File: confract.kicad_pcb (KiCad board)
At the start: 2 copper layers, 44 parts, among them J1 Conn_01x05, J10 GS2, J11 Conn_01x04, J12 GS2, J13 GS2, J14 GS2, J15 GS2, J16 Conn_01x02, J2 GS3, J3 Conn_01x05, J4 GS3, J5 Audio-Jack-4, J6 GS2, J7 GS2, J8 GS2, J9 GS3, Q1 Q_NMOS_GSD, SW1 SW_Push, SW10 SW_Push, SW11 SW_Push, SW12 SW_Push, SW13 SW_Push, SW14 SW_Push, SW15 SW_Push, SW16 SW_Push, SW17 SW_Push, SW2 SW_Push, SW3 SW_Push, SW4 SW_Push, SW5 SW_Push, SW6 SW_Push, SW7 SW_Push, SW8 SW_Push, SW9 SW_Push, U1 MCP23017_QFN

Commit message: load pcb-outline
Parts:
- moved J14 201.3 mm to (339.5, 76.8)
- moved J8 200.9 mm to (340.1, 87.0)
- moved J13 200.9 mm to (339.5, 80.2)
- moved J10 200.6 mm to (339.5, 83.6)
- moved J2 200.6 mm to (340.0, 91.1)
- moved C1 200.4 mm to (338.0, 71.8)
- moved U1 191.9 mm to (331.3, 92.4)
- moved SW2 190.5 mm to (328.7, 76.6)
- moved J6 188.5 mm to (328.1, 99.5)
- moved J1 181.2 mm to (320.6, 90.4)
- moved J4 177.7 mm to (316.8, 113.0)
- moved R6 177.6 mm to (317.1, 107.3)
- moved SW4 173.9 mm to (311.9, 76.6)
- moved Q1 172.0 mm to (309.7, 125.5)
- moved J5 170.6 mm to (310.2, 97.1)
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
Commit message: place components
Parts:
- J12, J13, J14, J15, J16: moved to B.Cu
- moved SW2 248.8 mm to (79.9, 70.0)
- moved SW4 234.1 mm to (80.0, 108.0)
- moved SW3 218.0 mm to (79.9, 89.0)
- moved J2 206.7 mm to (133.3, 93.3)
- moved C1 205.3 mm to (134.5, 98.5)
- moved U1 203.9 mm to (127.5, 98.5), turned to 135 degrees
- moved SW6 197.7 mm to (98.9, 89.0)
- moved SW5 186.0 mm to (99.0, 70.0)
- moved J4 181.3 mm to (136.5, 93.3)
- moved SW7 181.2 mm to (99.1, 108.0)
- moved SW9 177.7 mm to (117.9, 89.0)
- moved J14 169.9 mm to (173.4, 112.4)
- moved J13 166.8 mm to (175.9, 112.4)
- moved J8 166.2 mm to (175.9, 112.4), turned to 180 degrees
- moved J9 165.3 mm to (139.7, 93.3)
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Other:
- board outline added: 117.1 x 81 mm

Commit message: update schematic and pcb
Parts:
- moved R5 10.4 mm to (170.8, 95.2), turned to 270 degrees
- moved R4 9.91 mm to (167.0, 105.4), turned to 90 degrees
- turned Q1 to 180 degrees
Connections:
- U1 pad 2: SW13 -> SW15
- U1 pad 4: SW15 -> SW13
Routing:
- net GND: track 0.00 -> 490.1 mm, vias 0 -> 5
- net VCC: track 0.00 -> 168.2 mm, vias 0 -> 1
- net SDA: track 0.00 -> 102.3 mm, vias 0 -> 2
- net VBUS: track 0.00 -> 92.2 mm
- net SCL: track 0.00 -> 89.0 mm, vias 0 -> 2
- net RESET: track 0.00 -> 81.0 mm, vias 0 -> 1
- net SW0: track 0.00 -> 72.0 mm
- net Press: track 0.00 -> 70.5 mm, vias 0 -> 1
- net SW15: track 0.00 -> 60.4 mm
- net SW5: track 0.00 -> 59.1 mm
- net SW1: track 0.00 -> 55.5 mm
- net SW10: track 0.00 -> 51.0 mm
- net SW4: track 0.00 -> 46.4 mm
- net SW9: track 0.00 -> 41.1 mm
- net SW6: track 0.00 -> 39.8 mm
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- added copper zone on B.Cu, net GND
- added copper zone on F.Cu, net GND
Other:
- net class Power added: clearance 0.2, trace_width 0.5, via_dia 0.6, via_drill 0.4
- rule trace_min: 0.2 -> 0.25

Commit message: update silks
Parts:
- renumbered J9 to A0, J4 to A1, J2 to A2, J10 to GND, J15 to GND, J16 to PRESS, SW1 to RESET, J7 to SCL, J13 to SCL, J6 to SDA, J12 to SDA, J8 to VCC, J14 to VCC
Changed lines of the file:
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@@
     (46 B.CrtYd user)
     (47 F.CrtYd user)
-    (48 B.Fab user)
-    (49 F.Fab user)
+    (48 B.Fab user hide)
+    (49 F.Fab user hide)
   )
   (setup
@@
     (pad_to_mask_clearance 0.2)
     (aux_axis_origin 0 0)
-    (visible_elements FFFFFF1F)
+    (visible_elements 7FFFFFFF)
     (pcbplotparams
       (layerselection 0x00030_80000001)
@@
     (descr "C, Disc series, Radial, pin pitch=5.00mm, , diameter*width=4.3*1.9mm^2, Capacitor, http://www.vishay.com/docs/45233/krseries.pdf")
     (tags "C Disc series Radial pin pitch 5.00mm  diameter 4.3mm width 1.9mm Capacitor")
-    (fp_text reference C1 (at 2.5 -2.26) (layer F.SilkS)
+    (fp_text reference C1 (at 2.5 -0.075) (layer F.SilkS)
       (effects (font (size 1 1) (thickness 0.15)))
     )
@@
     (descr "Through hole straight socket strip, 1x05, 2.54mm pitch, single row")
     (tags "Through hole socket strip THT 1x05 2.54mm single row")
-    (fp_text reference J1 (at 0 -2.33) (layer F.SilkS)
+    (fp_text reference J1 (at 0 -2.33) (layer F.SilkS) hide
       (effects (font (size 1 1) (thickness 0.15)))
     )
@@
     (tags "solder bridge")
     (attr smd)
-    (fp_text reference J2 (at -1.7 0 90) (layer F.SilkS)
+    (fp_text reference A2 (at 0 3.175 180) (layer F.SilkS)
       (effects (font (size 1 1) (thickness 0.15)))
     )
@@
     (descr "Through hole straight socket strip, 1x05, 2.54mm pitch, single row")
     (tags "Through hole socket strip THT 1x05 2.54mm single row")
-    (fp_text reference J3 (at 0 -2.33 180) (layer F.SilkS)
+    (fp_text reference J3 (at 0 -2.33 180) (layer F.SilkS) hide
       (effects (font (size 1 1) (thickness 0.15)))
     )
@@
     (tags "solder bridge")
     (attr smd)
-    (fp_text reference J4 (at -1.7 0 90) (layer F.SilkS)
+    (fp_text reference A1 (at 0 3.175 180) (layer F.SilkS)
       (effects (font (size 1 1) (thickness 0.15)))
     )
@@
     (tags "solder bridge")
     (attr smd)
-    (fp_text reference J6 (at 1.78 0 270) (layer F.SilkS)
+    (fp_text reference SDA (at 0 -3.17 270) (layer F.SilkS)
       (effects (font (size 1 1) (thickness 0.15)))
     )
@@
     (tags "solder bridge")
     (attr smd)
-    (fp_text reference J7 (at 1.78 0 270) (layer F.SilkS)
+    (fp_text reference SCL (at 0 -3.17 270) (layer F.SilkS)
       (effects (font (size 1 1) (thickness 0.15)))
     )
@@
     (tags "solder bridge")
     (attr smd)
-    (fp_text reference J8 (at 1.78 0 270) (layer F.SilkS)
+    (fp_text reference VCC (at 0 -3.17 270) (layer F.SilkS)
       (effects (font (size 1 1) (thickness 0.15)))
     )
@@
     (tags "solder bridge")
     (attr smd)
-    (fp_text reference J9 (at -1.7 0 90) (layer F.SilkS)
+    (fp_text reference A0 (at 0 3.175 180) (layer F.SilkS)
       (effects (font (size 1 1) (thickness 0.15)))
     )
@@
     (tags "solder bridge")
     (attr smd)
-    (fp_text reference J10 (at 1.78 0 270) (layer F.SilkS)
+    (fp_text reference GND (at 0 -3.17 270) (layer F.SilkS)
       (effects (font (size 1 1) (thickness 0.15)))
     )
@@
     (tags "solder bridge")
     (attr smd)
-    (fp_text reference J12 (at 1.78 0 270) (layer B.SilkS)
+    (fp_text reference SDA (at 0 3.175 90) (layer B.SilkS)
       (effects (font (size 1 1) (thickness 0.15)) (justify mirror))
     )
@@
     (tags "solder bridge")
     (attr smd)
-    (fp_text reference J13 (at 1.78 0 270) (layer B.SilkS)
+    (fp_text reference SCL (at 0 3.175 90) (layer B.SilkS)
       (effects (font (size 1 1) (thickness 0.15)) (justify mirror))
     )
@@
     (tags "solder bridge")
     (attr smd)
-    (fp_text reference J14 (at 1.78 0 270) (layer B.SilkS)
+    (fp_text reference VCC (at 0 3.175 90) (layer B.SilkS)
       (effects (font (size 1 1) (thickness 0.15)) (justify mirror))
     )
@@
     (tags "solder bridge")
     (attr smd)
-    (fp_text reference J15 (at 1.78 0 270) (layer B.SilkS)
+    (fp_text reference GND (at 0 3.175 90) (layer B.SilkS)
       (effects (font (size 1 1) (thickness 0.15)) (justify mirror))
     )
@@
   (module footprint:FSR400 (layer B.Cu)
     (at 171.8287 135.773274 345)
-    (fp_text reference J16 (at -0.000001 -3.81 345) (layer B.SilkS)
+    (fp_text reference PRESS (at -0.000001 -3.81 345) (layer B.SilkS)
       (effects (font (size 1 1) (thickness 0.15)) (justify mirror))
     )
@@
     (descr "Resistor, Axial_DIN0207 series, Axial, Horizontal, pin pitch=10.16mm, 0.25W = 1/4W, length*diameter=6.3*2.5mm^2, http://cdn-reichelt.de/documents/datenblatt/B400/1_4W%23YAG.pdf")
     (tags "Resistor Axial_DIN0207 series Axial Horizontal pin pitch 10.16mm 0.25W = 1/4W length 6.3mm diameter 2.5mm")
-    (fp_text reference R1 (at 5.08 -2.31) (layer F.SilkS)
+    (fp_text reference R1 (at 5.08 0) (layer F.SilkS)
       (effects (font (size 1 1) (thickness 0.15)))
     )
@@
     (descr "Resistor, Axial_DIN0207 series, Axial, Horizontal, pin pitch=10.16mm, 0.25W = 1/4W, length*diameter=6.3*2.5mm^2, http://cdn-reichelt.de/documents/datenblatt/B400/1_4W%23YAG.pdf")
     (tags "Resistor Axial_DIN0207 series Axial Horizontal pin pitch 10.16mm 0.25W = 1/4W length 6.3mm diameter 2.5mm")
-    (fp_text reference R2 (at 5.08 -2.31 270) (layer F.SilkS)
+    (fp_text reference R2 (at 5.08 -0.254 270) (layer F.SilkS)
       (effects (font (size 1 1) (thickness 0.15)))
     )
@@
     (descr "Resistor, Axial_DIN0207 series, Axial, Horizontal, pin pitch=10.16mm, 0.25W = 1/4W, length*diameter=6.3*2.5mm^2, http://cdn-reichelt.de/documents/datenblatt/B400/1_4W%23YAG.pdf")
     (tags "Resistor Axial_DIN0207 series Axial Horizontal pin pitch 10.16mm 0.25W = 1/4W length 6.3mm diameter 2.5mm")
-    (fp_text reference R3 (at 5.08 -2.31 270) (layer F.SilkS)
+    (fp_text reference R3 (at 5.08 0.127 270) (layer F.SilkS)
       (effects (font (size 1 1) (thickness 0.15)))
     )
@@
     (descr "Resistor, Axial_DIN0207 series, Axial, Horizontal, pin pitch=10.16mm, 0.25W = 1/4W, length*diameter=6.3*2.5mm^2, http://cdn-reichelt.de/documents/datenblatt/B400/1_4W%23YAG.pdf")
     (tags "Resistor Axial_DIN0207 series Axial Horizontal pin pitch 10.16mm 0.25W = 1/4W length 6.3mm diameter 2.5mm")
-    (fp_text reference R4 (at 5.08 -2.31 90) (layer F.SilkS)
+    (fp_text reference R4 (at 5.08 0 90) (layer F.SilkS)
       (effects (font (size 1 1) (thickness 0.15)))
     )
@@
     (descr "Resistor, Axial_DIN0207 series, Axial, Horizontal, pin pitch=10.16mm, 0.25W = 1/4W, length*diameter=6.3*2.5mm^2, http://cdn-reichelt.de/documents/datenblatt/B400/1_4W%23YAG.pdf")
     (tags "Resistor Axial_DIN0207 series Axial Horizontal pin pitch 10.16mm 0.25W = 1/4W length 6.3mm diameter 2.5mm")
-    (fp_text reference R5 (at 5.08 -2.31 270) (layer F.SilkS)
+    (fp_text reference R5 (at 5.08 0 270) (layer F.SilkS)
       (effects (font (size 1 1) (thickness 0.15)))
     )
@@
     (descr "1x-dip-switch, Piano, row spacing 7.62 mm (300 mils)")
     (tags "DIP Switch Piano 7.62mm 300mil")
-    (fp_text reference SW1 (at 3.81 -3.17 270) (layer F.SilkS)
+    (fp_text reference RESET (at 3.81 0 270) (layer F.SilkS)
       (effects (font (size 1 1) (thickness 0.15)))
     )
@@
   (module footprint:MJ-4PP-9 (layer F.Cu)
     (at 179.5 101.14 270)
-    (fp_text reference J5 (at 0 7 270) (layer F.SilkS)
-      (effects (font (size 1 1) (thickness 0.15)))
-    )
+    (fp_text reference J5 (at 0.46 -0.205 270) (layer F.SilkS)
+      (effects (font (size 1 1) (thickness 0.15)))
+    )

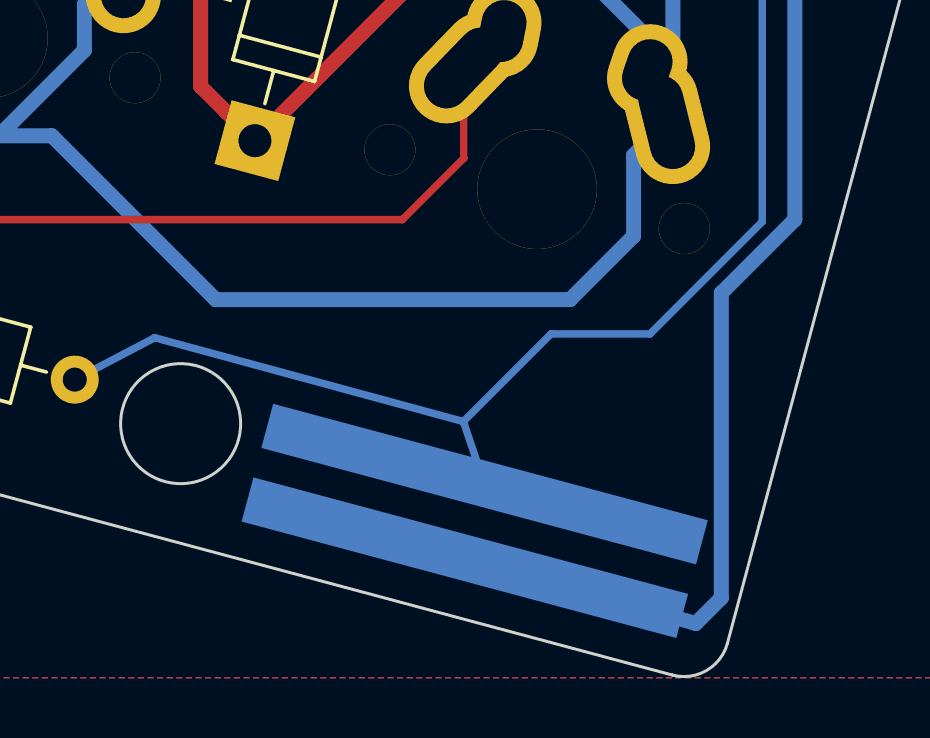
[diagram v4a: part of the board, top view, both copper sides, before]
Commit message: add logo silk
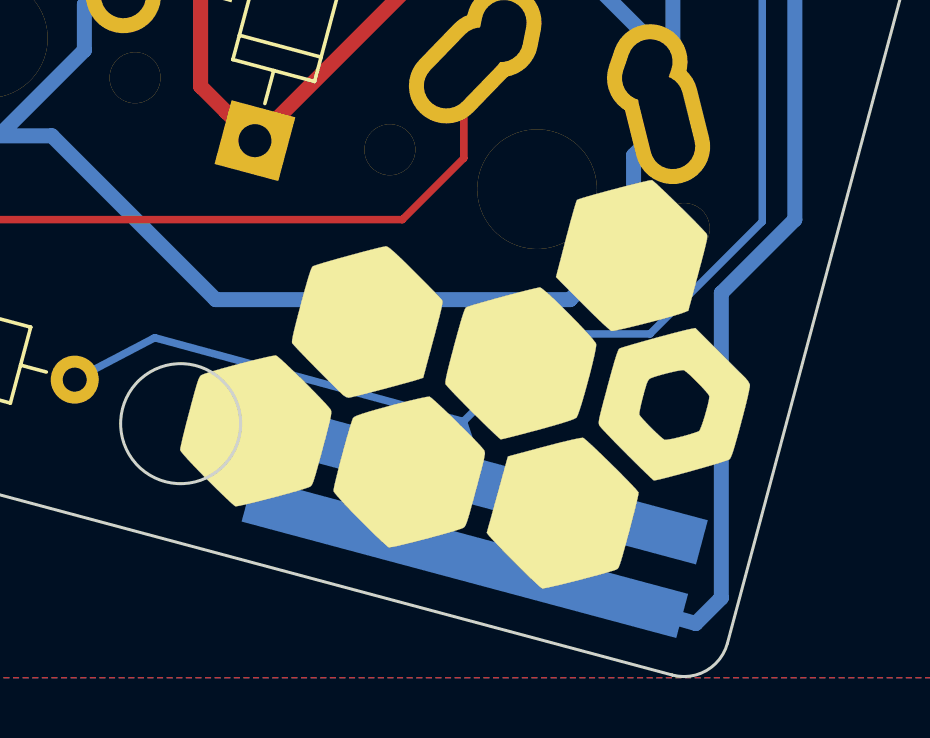
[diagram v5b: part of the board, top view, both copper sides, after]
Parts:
- added G***: LOGO, footprint:r2_logo, B.Cu at (154.3, 125.7)
- added G***: LOGO, footprint:r2_logo, F.Cu at (172.1, 130.2)
